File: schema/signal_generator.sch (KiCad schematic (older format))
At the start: 0 parts

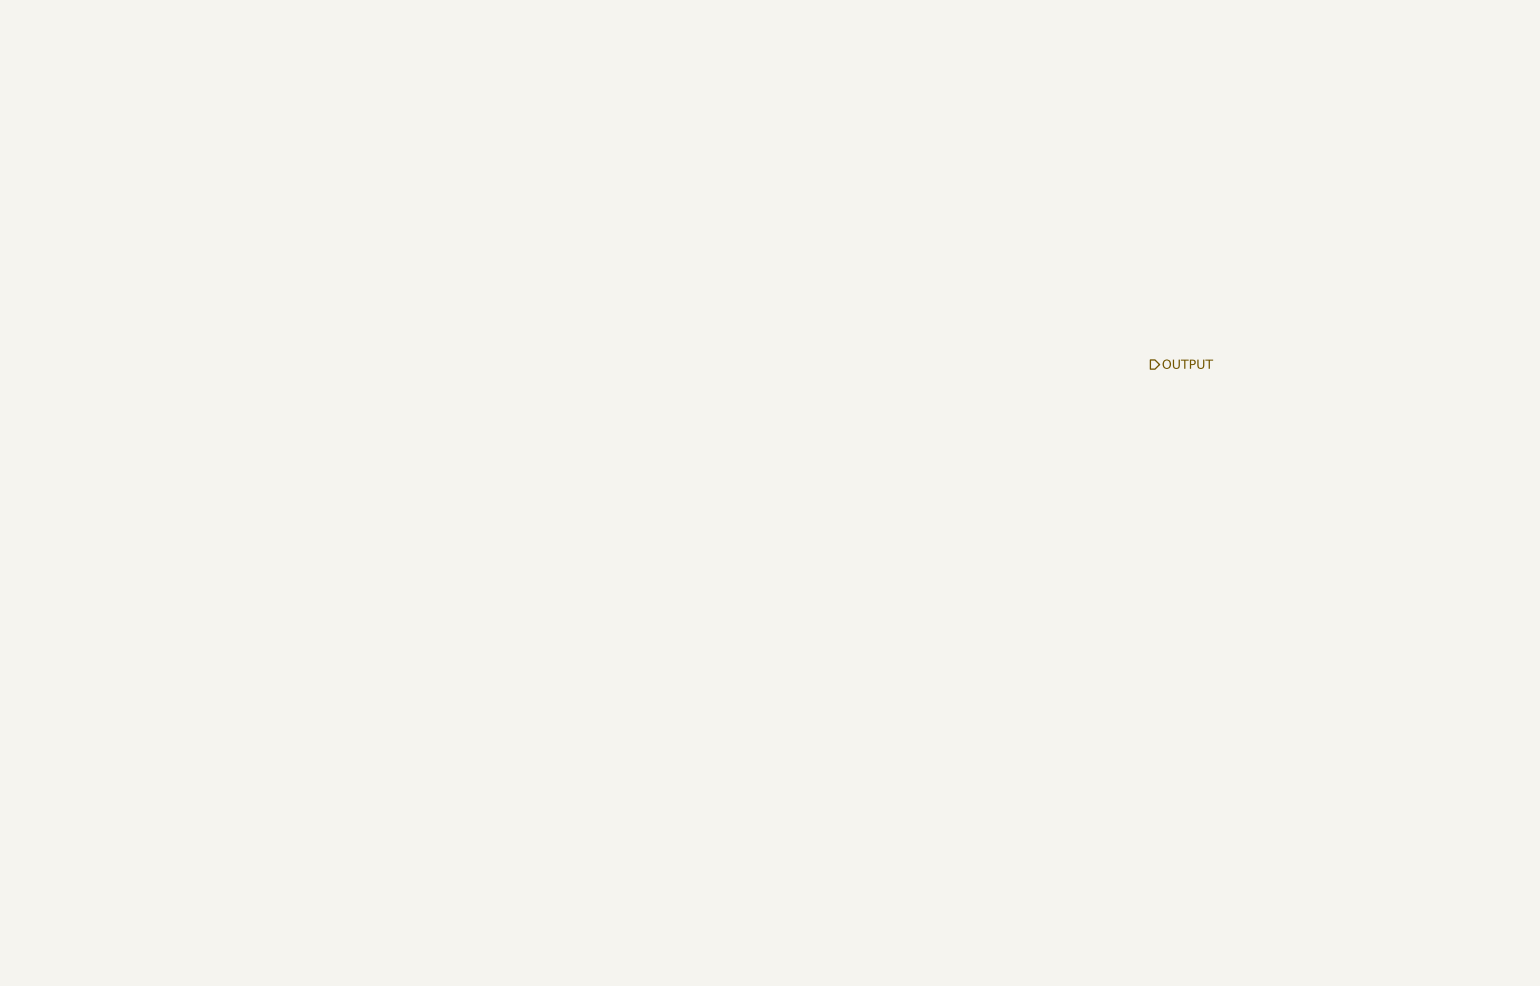
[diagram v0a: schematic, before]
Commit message: restore KiCAD _saved_* data
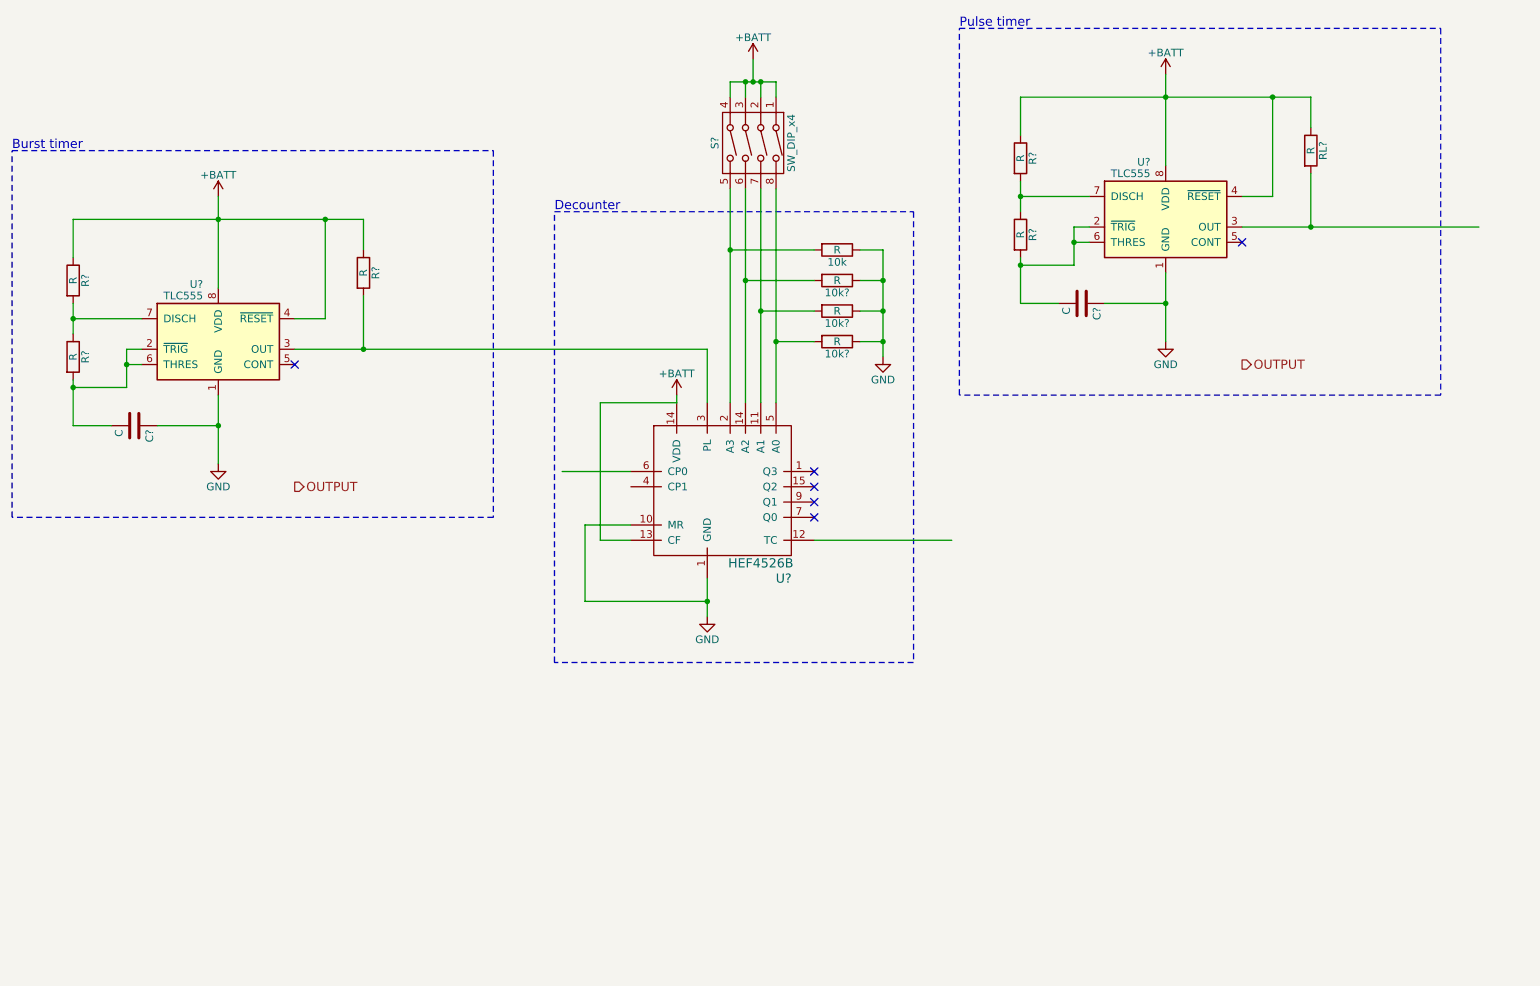
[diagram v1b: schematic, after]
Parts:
- added 10k, 10k? (x3), R? (x5), RL?: R, symbol R
- added C? (x2): C, symbol C
- added S?: SW_DIP_x4, symbol SW_DIP_x4
- added U?: HEF4526B, symbol HEF4526B
- added U? (x2): TLC555, symbol TLC555
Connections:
- net labels added: +BATT, GND
- wire segments 0 -> 66
- no-connect marks 0 -> 6
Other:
- note added: "Burst timer"
- note added: "Decounter"
- note added: "Pulse timer"

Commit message: decoder documentation
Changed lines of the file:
@@
 	2500 2750 2700 2750
 Wire Wire Line
-	2700 2100 2700 2750
+	2700 2750 2700 2100
 Wire Wire Line
 	1050 2100 2950 2100
@@
 	8700 1950 8900 1950
 Wire Wire Line
-	8900 1300 8900 1950
+	8900 1950 8900 1300
 Wire Wire Line
 	7250 1300 9150 1300

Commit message: filter and comparator
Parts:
- gave numbers to parts that had none: 15
- renumbered 10k to 10k1
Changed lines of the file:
@@
 LIBS:contrib
 LIBS:valves
+LIBS:custom
 LIBS:IRemote-cache
 EELAYER 25 0
@@
 OUTPUT
 $Comp
-L HEF4526B U?
+L HEF4526B U5
 U 1 1 5912CAA9
 P 5300 3850
-F 0 "U?" H 5700 3250 60  0000 C CNN
+F 0 "U5" H 5700 3250 60  0000 C CNN
 F 1 "HEF4526B" H 5550 3350 60  0000 C CNN
 F 2 "" H 5300 3850 60  0001 C CNN
@@
 $EndComp
 $Comp
-L TLC555 U?
+L TLC555 U4
 U 1 1 5912CB7D
 P 2000 2950
-F 0 "U?" H 1900 3375 50  0000 R CNN
+F 0 "U4" H 1900 3375 50  0000 R CNN
 F 1 "TLC555" H 1900 3300 50  0000 R CNN
 F 2 "" H 2050 2700 50  0000 L CNN
@@
 $EndComp
 $Comp
-L +BATT #PWR?
+L +BATT #PWR7
 U 1 1 5912CCA8
 P 5500 1050
-F 0 "#PWR?" H 5500 900 50  0001 C CNN
+F 0 "#PWR7" H 5500 900 50  0001 C CNN
 F 1 "+BATT" H 5500 1190 50  0000 C CNN
 F 2 "" H 5500 1050 50  0000 C CNN
@@
 NoConn ~ 5900 4050
 $Comp
-L SW_DIP_x4 S?
+L SW_DIP_x4 S2
 U 1 1 5912E74A
 P 5500 1600
-F 0 "S?" H 5500 1350 50  0000 C CNN
+F 0 "S2" H 5500 1350 50  0000 C CNN
 F 1 "SW_DIP_x4" H 5500 1850 50  0000 C CNN
 F 2 "" H 5450 1600 50  0000 C CNN
@@
 $EndComp
 $Comp
-L R 10k
+L R 10k1
 U 1 1 5912E962
 P 6050 2300
-F 0 "10k" V 6130 2300 50  0000 C CNN
+F 0 "10k1" V 6130 2300 50  0000 C CNN
 F 1 "R" V 6050 2300 50  0000 C CNN
 F 2 "" V 5980 2300 50  0000 C CNN
@@
 $EndComp
 $Comp
-L R 10k?
+L R 10k2
 U 1 1 5912EB18
 P 6050 2500
-F 0 "10k?" V 6130 2500 50  0000 C CNN
+F 0 "10k2" V 6130 2500 50  0000 C CNN
 F 1 "R" V 6050 2500 50  0000 C CNN
 F 2 "" V 5980 2500 50  0000 C CNN
@@
 $EndComp
 $Comp
-L R 10k?
+L R 10k3
 U 1 1 5912EC70
 P 6050 2700
-F 0 "10k?" V 6130 2700 50  0000 C CNN
+F 0 "10k3" V 6130 2700 50  0000 C CNN
 F 1 "R" V 6050 2700 50  0000 C CNN
 F 2 "" V 5980 2700 50  0000 C CNN
@@
 $EndComp
 $Comp
-L R 10k?
+L R 10k4
 U 1 1 5912ECA5
 P 6050 2900
-F 0 "10k?" V 6130 2900 50  0000 C CNN
+F 0 "10k4" V 6130 2900 50  0000 C CNN
 F 1 "R" V 6050 2900 50  0000 C CNN
 F 2 "" V 5980 2900 50  0000 C CNN
@@
 $EndComp
 $Comp
-L GND #PWR?
+L GND #PWR8
 U 1 1 5912ED7F
 P 6350 3000
-F 0 "#PWR?" H 6350 2750 50  0001 C CNN
+F 0 "#PWR8" H 6350 2750 50  0001 C CNN
 F 1 "GND" H 6350 2850 50  0000 C CNN
 F 2 "" H 6350 3000 50  0000 C CNN
@@
 $EndComp
 $Comp
-L GND #PWR?
+L GND #PWR6
 U 1 1 59130203
 P 5200 4700
-F 0 "#PWR?" H 5200 4450 50  0001 C CNN
+F 0 "#PWR6" H 5200 4450 50  0001 C CNN
 F 1 "GND" H 5200 4550 50  0000 C CNN
 F 2 "" H 5200 4700 50  0000 C CNN
@@
 	5200 4450 5200 4700
 $Comp
-L +BATT #PWR?
+L +BATT #PWR5
 U 1 1 591303F3
 P 5000 3250
-F 0 "#PWR?" H 5000 3100 50  0001 C CNN
+F 0 "#PWR5" H 5000 3100 50  0001 C CNN
 F 1 "+BATT" H 5000 3390 50  0000 C CNN
 F 2 "" H 5000 3250 50  0000 C CNN
@@
 	4500 4200 4700 4200
 $Comp
-L +BATT #PWR?
+L +BATT #PWR3
 U 1 1 591329F1
 P 2000 1950
-F 0 "#PWR?" H 2000 1800 50  0001 C CNN
+F 0 "#PWR3" H 2000 1800 50  0001 C CNN
 F 1 "+BATT" H 2000 2090 50  0000 C CNN
 F 2 "" H 2000 1950 50  0000 C CNN
@@
 Connection ~ 1400 3050
 $Comp
-L R R?
+L R R10
 U 1 1 59132C26
 P 1050 3000
-F 0 "R?" V 1130 3000 50  0000 C CNN
+F 0 "R10" V 1130 3000 50  0000 C CNN
 F 1 "R" V 1050 3000 50  0000 C CNN
 F 2 "" V 980 3000 50  0000 C CNN
@@
 Connection ~ 2000 2100
 $Comp
-L R R?
+L R R11
 U 1 1 59132D4D
 P 2950 2450
-F 0 "R?" V 3030 2450 50  0000 C CNN
+F 0 "R11" V 3030 2450 50  0000 C CNN
 F 1 "R" V 2950 2450 50  0000 C CNN
 F 2 "" V 2880 2450 50  0000 C CNN
@@
 Connection ~ 2950 2950
 $Comp
-L GND #PWR?
+L GND #PWR4
 U 1 1 59132E59
 P 2000 3700
-F 0 "#PWR?" H 2000 3450 50  0001 C CNN
+F 0 "#PWR4" H 2000 3450 50  0001 C CNN
 F 1 "GND" H 2000 3550 50  0000 C CNN
 F 2 "" H 2000 3700 50  0000 C CNN
@@
 NoConn ~ 2500 3050
 $Comp
-L R R?
+L R R9
 U 1 1 59133297
 P 1050 2500
-F 0 "R?" V 1130 2500 50  0000 C CNN
+F 0 "R9" V 1130 2500 50  0000 C CNN
 F 1 "R" V 1050 2500 50  0000 C CNN
 F 2 "" V 980 2500 50  0000 C CNN
@@
 	1400 3200 1050 3200
 $Comp
-L C C?
+L C C5
 U 1 1 5913391D
 P 1450 3450
-F 0 "C?" H 1475 3550 50  0000 L CNN
+F 0 "C5" H 1475 3550 50  0000 L CNN
 F 1 "C" H 1475 3350 50  0000 L CNN
 F 2 "" H 1488 3300 50  0000 C CNN
@@
 OUTPUT
 $Comp
-L TLC555 U?
+L TLC555 U6
 U 1 1 5913C644
 P 8200 2150
-F 0 "U?" H 8100 2575 50  0000 R CNN
+F 0 "U6" H 8100 2575 50  0000 R CNN
 F 1 "TLC555" H 8100 2500 50  0000 R CNN
 F 2 "" H 8250 1900 50  0000 L CNN
@@
 $EndComp
 $Comp
-L +BATT #PWR?
+L +BATT #PWR9
 U 1 1 5913C64A
 P 8200 1150
-F 0 "#PWR?" H 8200 1000 50  0001 C CNN
+F 0 "#PWR9" H 8200 1000 50  0001 C CNN
 F 1 "+BATT" H 8200 1290 50  0000 C CNN
 F 2 "" H 8200 1150 50  0000 C CNN
@@
 Connection ~ 7600 2250
 $Comp
-L R R?
+L R R13
 U 1 1 5913C657
 P 7250 2200
-F 0 "R?" V 7330 2200 50  0000 C CNN
+F 0 "R13" V 7330 2200 50  0000 C CNN
 F 1 "R" V 7250 2200 50  0000 C CNN
 F 2 "" V 7180 2200 50  0000 C CNN
@@
 	8700 2150 10250 2150
 $Comp
-L R RL?
+L R RL1
 U 1 1 5913C665
 P 9150 1650
-F 0 "RL?" V 9230 1650 50  0000 C CNN
+F 0 "RL1" V 9230 1650 50  0000 C CNN
 F 1 "R" V 9150 1650 50  0000 C CNN
 F 2 "" V 9080 1650 50  0000 C CNN
@@
 Connection ~ 9150 2150
 $Comp
-L GND #PWR?
+L GND #PWR10
 U 1 1 5913C66F
 P 8200 2900
-F 0 "#PWR?" H 8200 2650 50  0001 C CNN
+F 0 "#PWR10" H 8200 2650 50  0001 C CNN
 F 1 "GND" H 8200 2750 50  0000 C CNN
 F 2 "" H 8200 2900 50  0000 C CNN
@@
 NoConn ~ 8700 2250
 $Comp
-L R R?
+L R R12
 U 1 1 5913C678
 P 7250 1700
-F 0 "R?" V 7330 1700 50  0000 C CNN
+F 0 "R12" V 7330 1700 50  0000 C CNN
 F 1 "R" V 7250 1700 50  0000 C CNN
 F 2 "" V 7180 1700 50  0000 C CNN
@@
 	7600 2400 7250 2400
 $Comp
-L C C?
+L C C6
 U 1 1 5913C686
 P 7650 2650
-F 0 "C?" H 7675 2750 50  0000 L CNN
+F 0 "C6" H 7675 2750 50  0000 L CNN
 F 1 "C" H 7675 2550 50  0000 L CNN
 F 2 "" H 7688 2500 50  0000 C CNN

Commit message: Signal generator
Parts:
- added U? (x4): 7402, symbol 7402
- RL1: renamed from 10k4; value R -> 10k
- RL2: renamed from 10k3; value R -> 10k
- RL3: renamed from 10k2; value R -> 10k
- RL4: renamed from 10k1; value R -> 10k
- renumbered R13 to 1.5k, C6 to 100nF, R12 to 11.5k, R10 to 433k, R9 to 577k, C5 to C?, R11 to R?, RL1 to RL?, S2 to S?, U5 to U?, U4 to U?, U6 to U?
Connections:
- wire segments 66 -> 109
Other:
- note added: "Burst timer (th = 70ms, tl = 30ms)"
- note added: "Pulse timer (th = 100us, tl= 900us)"
- note removed: "Burst timer"
- note removed: "Pulse timer"
- moved on the sheet: 1.5k, 100nF, 11.5k, RL1, RL2, RL3, RL4, RL?, S?, U?

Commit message: ouput driver
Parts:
- 11.5k: value R -> 12k
- 433k: value R -> 467k
- 577k: value R -> 556k
- U? (x4): symbol 7402 -> 7402-RESCUE-IRemote
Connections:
- wire segments 109 -> 81
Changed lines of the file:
@@
 P 1050 3000
 F 0 "433k" V 1130 3000 50  0000 C CNN
-F 1 "R" V 1050 3000 50  0000 C CNN
+F 1 "467k" V 1050 3000 50  0000 C CNN
 F 2 "" V 980 3000 50  0000 C CNN
 F 3 "" H 1050 3000 50  0000 C CNN
@@
 P 1050 2500
 F 0 "577k" V 1130 2500 50  0000 C CNN
-F 1 "R" V 1050 2500 50  0000 C CNN
+F 1 "556k" V 1050 2500 50  0000 C CNN
 F 2 "" V 980 2500 50  0000 C CNN
 F 3 "" H 1050 2500 50  0000 C CNN
@@
 P 1050 5400
 F 0 "11.5k" V 1130 5400 50  0000 C CNN
-F 1 "R" V 1050 5400 50  0000 C CNN
+F 1 "12k" V 1050 5400 50  0000 C CNN
 F 2 "" V 980 5400 50  0000 C CNN
 F 3 "" H 1050 5400 50  0000 C CNN
@@
 Pulse timer (th = 100us, tl= 900us)
 $Comp
-L 7402 U?
+L 7402-RESCUE-IRemote U?
 U 1 1 591D57A6
 P 5300 5400
+AR Path="/591D57A6" Ref="U?"  Part="1"
+AR Path="/5910364F/591D57A6" Ref="U?"  Part="1"
 F 0 "U?" H 5300 5450 50  0000 C CNN
 F 1 "7402" H 5350 5350 50  0000 C CNN
@@
 $EndComp
 $Comp
-L 7402 U?
+L 7402-RESCUE-IRemote U?
 U 1 1 591D7115
 P 6700 5500
+AR Path="/591D7115" Ref="U?"  Part="1"
+AR Path="/5910364F/591D7115" Ref="U?"  Part="1"
 F 0 "U?" H 6700 5550 50  0000 C CNN
 F 1 "7402" H 6750 5450 50  0000 C CNN
@@
 $EndComp
 $Comp
-L 7402 U?
+L 7402-RESCUE-IRemote U?
 U 1 1 591D774A
 P 8800 5400
+AR Path="/591D774A" Ref="U?"  Part="1"
+AR Path="/5910364F/591D774A" Ref="U?"  Part="1"
 F 0 "U?" H 8800 5450 50  0000 C CNN
 F 1 "7402" H 8850 5350 50  0000 C CNN
@@
 	6600 1300 6600 1200
 Wire Wire Line
-	6600 1200 6700 1200
-Wire Wire Line
-	6700 1200 6750 1200
-Wire Wire Line
-	6750 1200 6800 1200
-Wire Wire Line
-	6800 1200 6900 1200
+	6600 1200 6900 1200
 Wire Wire Line
 	6900 1200 6900 1300
@@
 Connection ~ 6750 1200
 Wire Wire Line
-	6600 1900 6600 2300
-Wire Wire Line
-	6600 2300 6600 3300
-Wire Wire Line
-	6700 1900 6700 2500
-Wire Wire Line
-	6700 2500 6700 3300
-Wire Wire Line
-	6800 1900 6800 2700
-Wire Wire Line
-	6800 2700 6800 3300
-Wire Wire Line
-	6900 1900 6900 2900
-Wire Wire Line
-	6900 2900 6900 3300
+	6600 1900 6600 3300
+Wire Wire Line
+	6700 1900 6700 3300
+Wire Wire Line
+	6800 1900 6800 3300
+Wire Wire Line
+	6900 1900 6900 3300
 Wire Wire Line
 	6600 2300 7150 2300
@@
 	7450 2300 7600 2300
 Wire Wire Line
-	7600 2300 7600 2500
-Wire Wire Line
-	7600 2500 7600 2700
-Wire Wire Line
-	7600 2700 7600 2900
-Wire Wire Line
-	7600 2900 7600 3000
+	7600 2300 7600 3000
 Wire Wire Line
 	7600 2900 7450 2900
@@
 Connection ~ 7600 2900
 Wire Wire Line
-	6450 4450 6450 4600
-Wire Wire Line
-	6450 4600 6450 4700
+	6450 4450 6450 4700
 Wire Wire Line
 	6250 3300 6250 3250
@@
 	6450 2950 6450 3300
 Wire Wire Line
-	2500 2950 2950 2950
-Wire Wire Line
-	2950 2950 4350 2950
-Wire Wire Line
-	4350 2950 6450 2950
+	2500 2950 6450 2950
 Wire Wire Line
 	5950 3750 5500 3750
@@
 	5750 4200 5950 4200
 Wire Wire Line
-	2000 1950 2000 2100
-Wire Wire Line
-	2000 2100 2000 2550
+	2000 1950 2000 2550
 Wire Wire Line
 	1500 2950 1400 2950
 Wire Wire Line
-	1400 2950 1400 3050
-Wire Wire Line
-	1400 3050 1400 3200
+	1400 2950 1400 3200
 Wire Wire Line
 	1400 3050 1500 3050
@@
 	2500 2750 2700 2750
 Wire Wire Line
-	2700 2750 2700 2100
-Wire Wire Line
-	1050 2100 2000 2100
-Wire Wire Line
-	2000 2100 2700 2100
-Wire Wire Line
-	2700 2100 2950 2100
+	2700 2100 2700 2750
+Wire Wire Line
+	1050 2100 2950 2100
 Connection ~ 2000 2100
 Wire Wire Line
@@
 Connection ~ 2950 2950
 Wire Wire Line
-	2000 3250 2000 3450
-Wire Wire Line
-	2000 3450 2000 3700
-Wire Wire Line
-	1050 2650 1050 2750
-Wire Wire Line
-	1050 2750 1050 2850
+	2000 3250 2000 3700
+Wire Wire Line
+	1050 2650 1050 2850
 Wire Wire Line
 	1050 2750 1500 2750
@@
 	1050 2100 1050 2350
 Wire Wire Line
-	1050 3150 1050 3200
-Wire Wire Line
-	1050 3200 1050 3450
+	1050 3150 1050 3450
 Wire Wire Line
 	1400 3200 1050 3200
@@
 	7800 5000 5450 5000
 Wire Wire Line
-	2000 4850 2000 5000
-Wire Wire Line
-	2000 5000 2000 5450
+	2000 4850 2000 5450
 Wire Wire Line
 	1500 5850 1400 5850
 Wire Wire Line
-	1400 5850 1400 5950
-Wire Wire Line
-	1400 5950 1400 6100
+	1400 5850 1400 6100
 Wire Wire Line
 	1400 5950 1500 5950
@@
 	2500 5650 2700 5650
 Wire Wire Line
-	1050 5000 2000 5000
-Wire Wire Line
-	2000 5000 2950 5000
+	1050 5000 2950 5000
 Connection ~ 2000 5000
 Wire Wire Line
-	2500 5850 2950 5850
-Wire Wire Line
-	2950 5850 4350 5850
+	2500 5850 4350 5850
 Wire Wire Line
 	2950 5000 2950 5200
@@
 Connection ~ 2950 5850
 Wire Wire Line
-	2000 6150 2000 6350
-Wire Wire Line
-	2000 6350 2000 6600
-Wire Wire Line
-	1050 5550 1050 5650
-Wire Wire Line
-	1050 5650 1050 5750
+	2000 6150 2000 6600
+Wire Wire Line
+	1050 5550 1050 5750
 Wire Wire Line
 	1050 5650 1500 5650
@@
 	1050 5000 1050 5250
 Wire Wire Line
-	1050 6050 1050 6100
-Wire Wire Line
-	1050 6100 1050 6350
+	1050 6050 1050 6350
 Wire Wire Line
 	1400 6100 1050 6100
@@
 	2700 6450 4950 6450
 $Comp
-L 7402 U?
+L 7402-RESCUE-IRemote U?
 U 1 1 591D82E2
 P 5550 6450
+AR Path="/591D82E2" Ref="U?"  Part="1"
+AR Path="/5910364F/591D82E2" Ref="U?"  Part="1"
 F 0 "U?" H 5550 6500 50  0000 C CNN
 F 1 "7402" H 5600 6400 50  0000 C CNN
@@
 Connection ~ 4350 2950
 Wire Wire Line
-	7900 4200 7900 5300
-Wire Wire Line
-	7900 5300 7900 6350
+	7900 4200 7900 6350
 Wire Wire Line
 	7900 6350 6150 6350
